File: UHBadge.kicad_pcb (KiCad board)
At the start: 2 copper layers, 70 x 117.6 mm, 91 parts, among them J1 Conn_01x03_MountingPin, J2 Conn_01x10_MountingPin, J3 LEMO2, P1 USB_C_Plug_USB2.0, Q1 Si1308EDL, SW1 Boot, SW2 Run, SW3 Up, SW4 Down, SW5 Left, SW6 Right, U1 RP2350A, U2 MCP73871, U3 W25Q128JVS, U4 SRV05-4, U5 Conn, U6 ST25DV64K-JFR6D3, U7 Radio Module 2, Y1 ABM8-272-T3

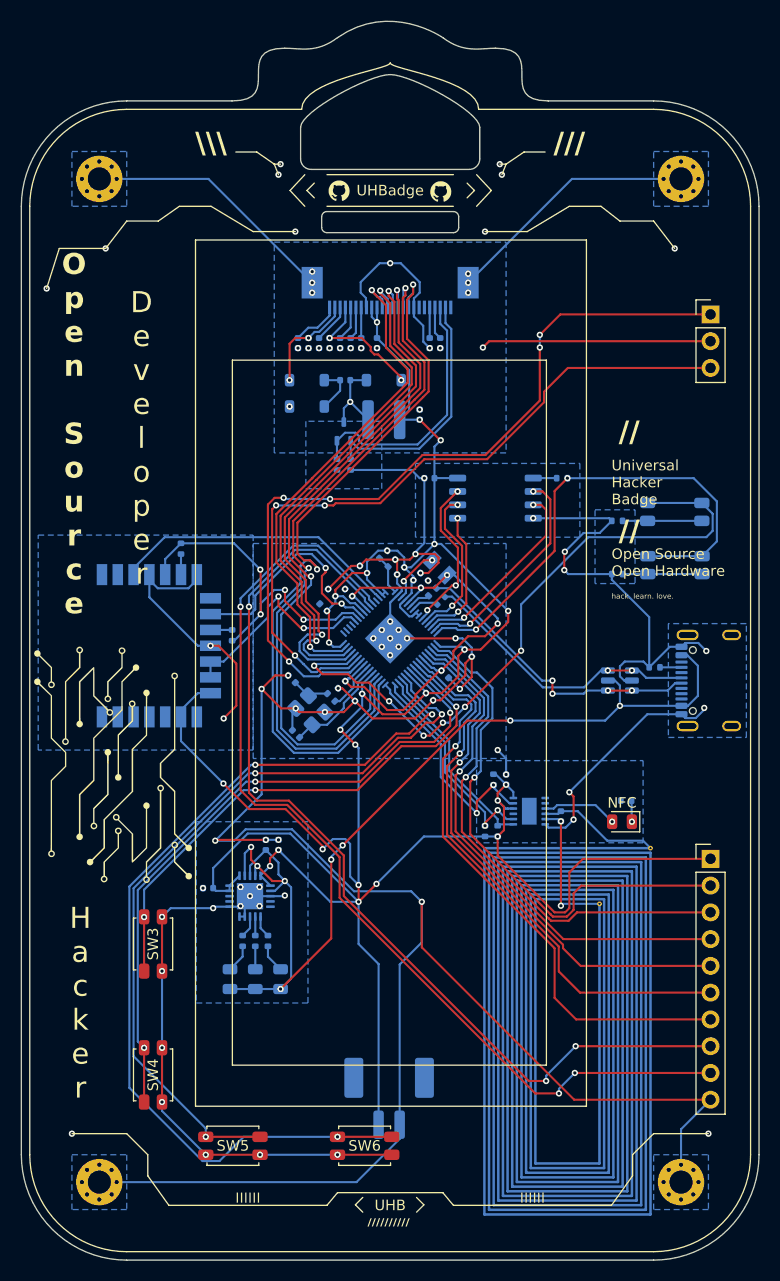
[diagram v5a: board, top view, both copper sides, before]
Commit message: Added the microSD card slot. Moved the SW pins. Removed two expansion pins. Added some graphical designs.
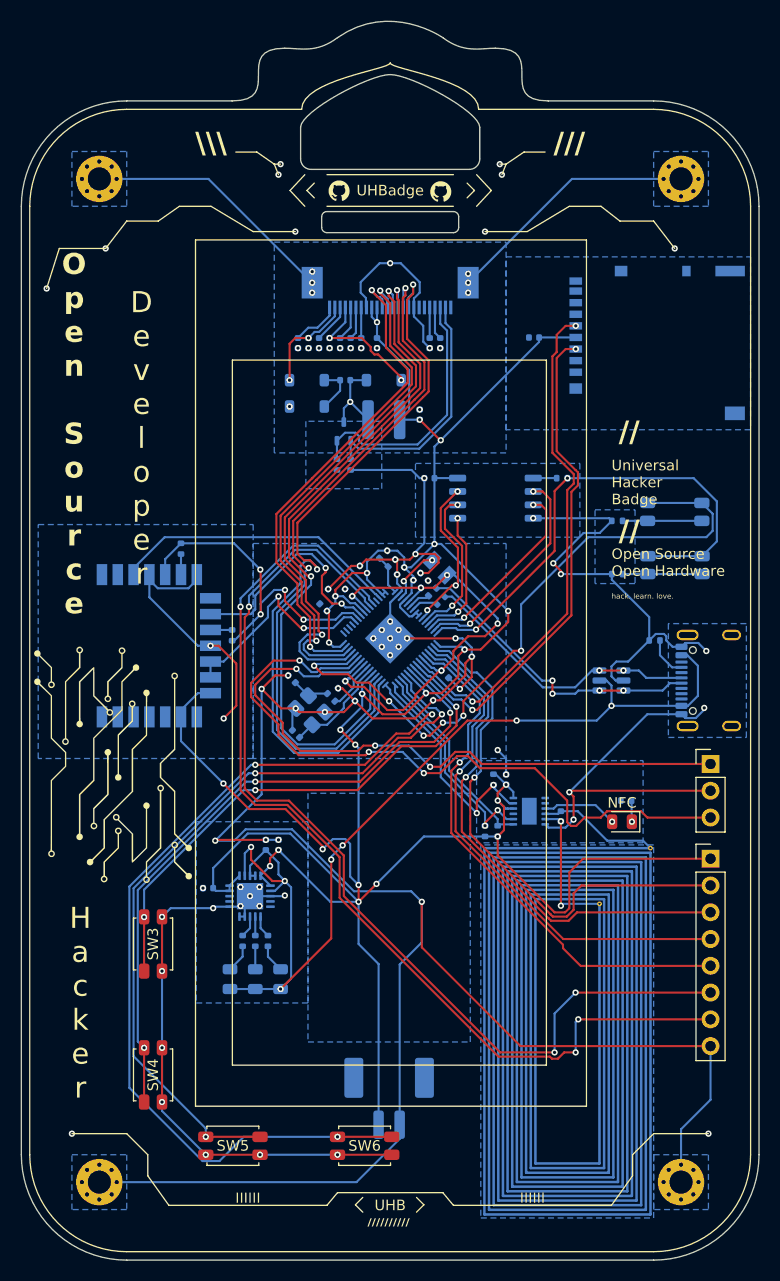
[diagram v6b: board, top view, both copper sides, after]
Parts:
- removed J2: Conn_01x10_MountingPin, Connector_PinHeader_2.54mm:PinHeader_1x10_P2.54mm_Vertical
- added C36: 10uF, Capacitor_SMD:C_0402_1005Metric, B.Cu at (148.7, 72.5)
- added G***: LOGO, LOGO, B.Cu at (116.2, 145.3)
- added G***: LOGO, LOGO, B.Cu at (112.0, 145.2)
- added G***: LOGO, LOGO, B.Cu at (112.0, 140.6)
- added G***: LOGO, LOGO, B.Cu at (107.4, 145.2)
- added G***: LOGO, LOGO, B.Cu at (114.0, 142.8)
- added G***: LOGO, LOGO, B.Cu at (107.4, 140.6)
- added G***: LOGO, LOGO, B.Cu at (120.8, 140.6)
- added G***: LOGO, LOGO, B.Cu at (116.2, 140.6)
- added J4: Micro_SD_Card, Connector_Card:microSD_HC_Hirose_DM3AT-SF-PEJM5, B.Cu at (160.3, 73.0)
- added J5: Conn_01x08_MountingPin, Connector_PinHeader_2.54mm:PinHeader_1x08_P2.54mm_Vertical, F.Cu at (165.4, 121.9)
- moved J1 42.7 mm to (165.4, 112.9)
- moved G*** 9.00 mm to (160.0, 105.0), turned to 90 degrees
- moved R4 2.55 mm to (160.1, 101.2)
- moved U4 0.80 mm to (156.0, 105.0)
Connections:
- U1 pad 31: unconnected-(U1-GPIO19-Pad31) -> SD-DAT0
- U1 pad 32: unconnected-(U1-GPIO20-Pad32) -> SD-DAT1
- U1 pad 33: unconnected-(U1-GPIO21-Pad33) -> SD-DAT2
- U1 pad 34: unconnected-(U1-GPIO22-Pad34) -> SD-DAT3
- U1 pad 7: GPIO4 -> SD-CLK
- U1 pad 8: GPIO5 -> SD-CMD
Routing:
- net GPIO5: track 55.9 -> 0.00 mm, vias 1 -> 0
- net GPIO4: track 53.3 -> 0.00 mm, vias 1 -> 0
- net SD-CLK: track 0.00 -> 49.0 mm, vias 0 -> 2
- net SD-CMD: track 0.00 -> 48.0 mm, vias 0 -> 2
- net +3V3: track 270.4 -> 287.5 mm
- net SWCLK: track 77.0 -> 60.7 mm, vias 5 -> 3
- net -BATT: track 461.6 -> 456.5 mm, vias 78 -> 77
- net SWDIO: track 69.8 -> 66.3 mm
- net ADC0: track 93.5 -> 95.5 mm
- net Net-(P1-CC): track 2.05 -> 3.92 mm
- net ADC1: track 95.2 -> 96.0 mm
- net RUN: track 63.8 -> 64.6 mm
- net USB_C_VBUS: track 97.6 -> 97.1 mm, vias 8 -> 7
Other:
- board text added: "Hack the Planet"

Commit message: Fixed some little graphical details.
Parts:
- added G***: LOGO, LOGO, F.Cu at (165.0, 105.0)
- added G***: LOGO, LOGO, B.Cu at (120.8, 144.1)
- moved G*** 1.20 mm to (116.2, 144.1)
- moved G*** 1.20 mm to (114.0, 141.6)
- moved G*** 1.20 mm to (116.2, 139.4)
- moved G*** 1.20 mm to (112.0, 144.0)
- moved G*** 1.20 mm to (112.0, 139.4)
- moved G*** 1.20 mm to (107.4, 144.0)
- moved G*** 1.20 mm to (107.4, 139.4)
- moved G*** 1.20 mm to (120.8, 139.4)
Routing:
- net ADC1: track 96.0 -> 99.0 mm
- net ADC0: track 95.5 -> 96.2 mm
